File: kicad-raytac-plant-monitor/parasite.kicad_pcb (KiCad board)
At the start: 4 copper layers, 30 x 126.4 mm, 36 parts, among them J1 Cortex SWD 10-pin, J2 I2C 3V, J3 NFC ANTENNA, Q1 MMBT3906, Q4 Q_Photo_NPN, SW1 B3U-1000P, U1 MDBT50Q-1MV2, U2 SHTC3, Y1 32.768kHz

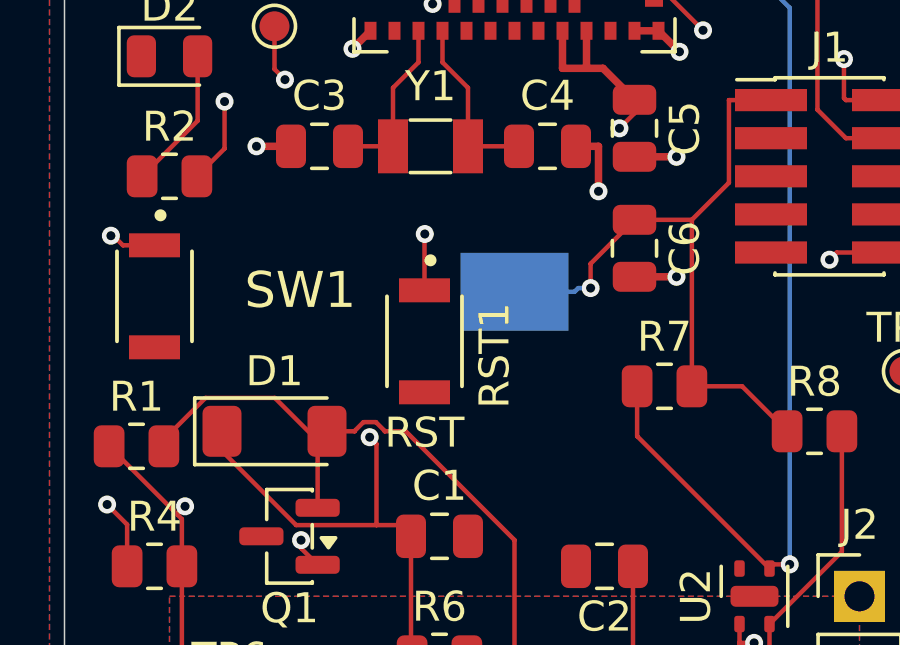
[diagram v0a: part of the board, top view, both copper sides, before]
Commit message: feat: align Raytac user and reset buttons horizontally
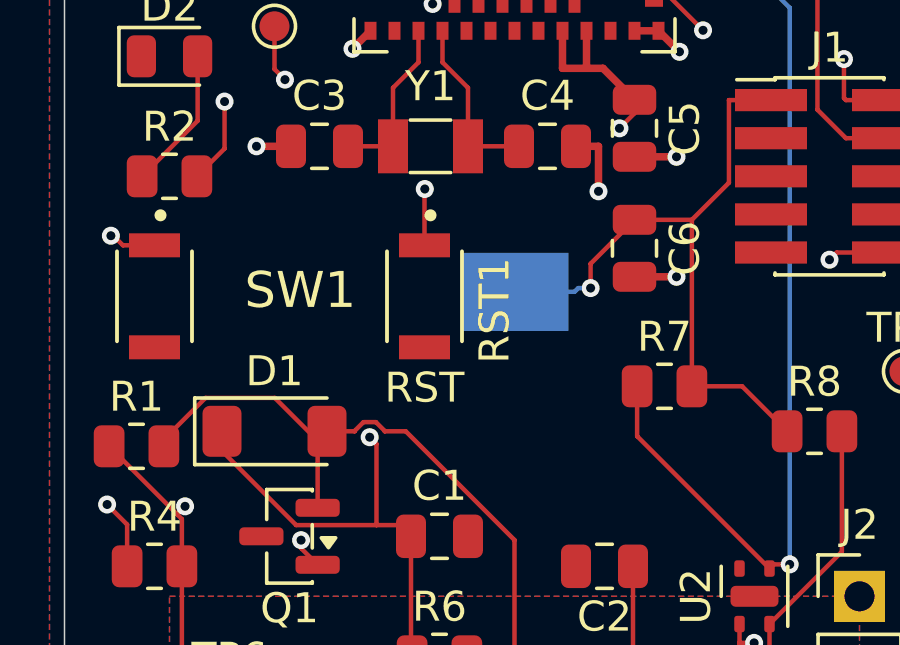
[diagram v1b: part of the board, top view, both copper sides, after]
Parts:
- moved RST1 1.50 mm to (65.0, 51.0)
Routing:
- net RST: track 35.8 -> 34.3 mm
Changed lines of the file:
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@@
 	(footprint "snapeda:SW_B3U-1000P"
 		(layer "F.Cu")
-		(at 65 52.5 -90)
+		(at 65 51 -90)
 		(property "Reference" "RST1"
 			(at 0.475 -2.335 270)
@@
 		(sheetname "/")
 		(sheetfile "parasite.kicad_sch")
-		(units
-			(unit
-				(name "A")
-				(pins "1" "2")
-			)
-		)
 		(attr smd)
 		(duplicate_pad_numbers_are_jumpers no)
@@
 	)
 	(segment
+		(start 65.0098 47.4231)
+		(end 65 47.4329)
+		(width 0.15)
+		(layer "F.Cu")
+		(net "RST")
+	)
+	(segment
 		(start 80.45 49.54)
 		(end 81.8517 49.54)
@@
 	)
 	(segment
+		(start 65 47.4329)
+		(end 65 49.3)
+		(width 0.15)
+		(layer "F.Cu")
+		(net "RST")
+	)
+	(segment
 		(start 80.45 49.54)
 		(end 78.7402 49.54)
@@
 		(net "RST")
 	)
-	(segment
-		(start 65 48.9329)
-		(end 65 50.8)
-		(width 0.15)
-		(layer "F.Cu")
-		(net "RST")
-	)
-	(segment
-		(start 65.0098 48.9231)
-		(end 65 48.9329)
-		(width 0.15)
-		(layer "F.Cu")
-		(net "RST")
-	)
 	(via
-		(at 65.0098 48.9231)
+		(at 65.0098 47.4231)
 		(size 0.6)
 		(drill 0.3)
@@
 	)
 	(segment
-		(start 69.6228 41.0493)
-		(end 65.0098 45.6623)
+		(start 65.0098 45.6623)
+		(end 65.0098 47.4231)
 		(width 0.15)
 		(layer "In2.Cu")
@@
 	)
 	(segment
-		(start 65.0098 45.6623)
-		(end 65.0098 48.9231)
+		(start 69.6228 41.0493)
+		(end 65.0098 45.6623)
 		(width 0.15)
 		(layer "In2.Cu")
